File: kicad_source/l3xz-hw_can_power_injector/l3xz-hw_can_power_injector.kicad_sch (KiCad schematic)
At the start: 6 parts

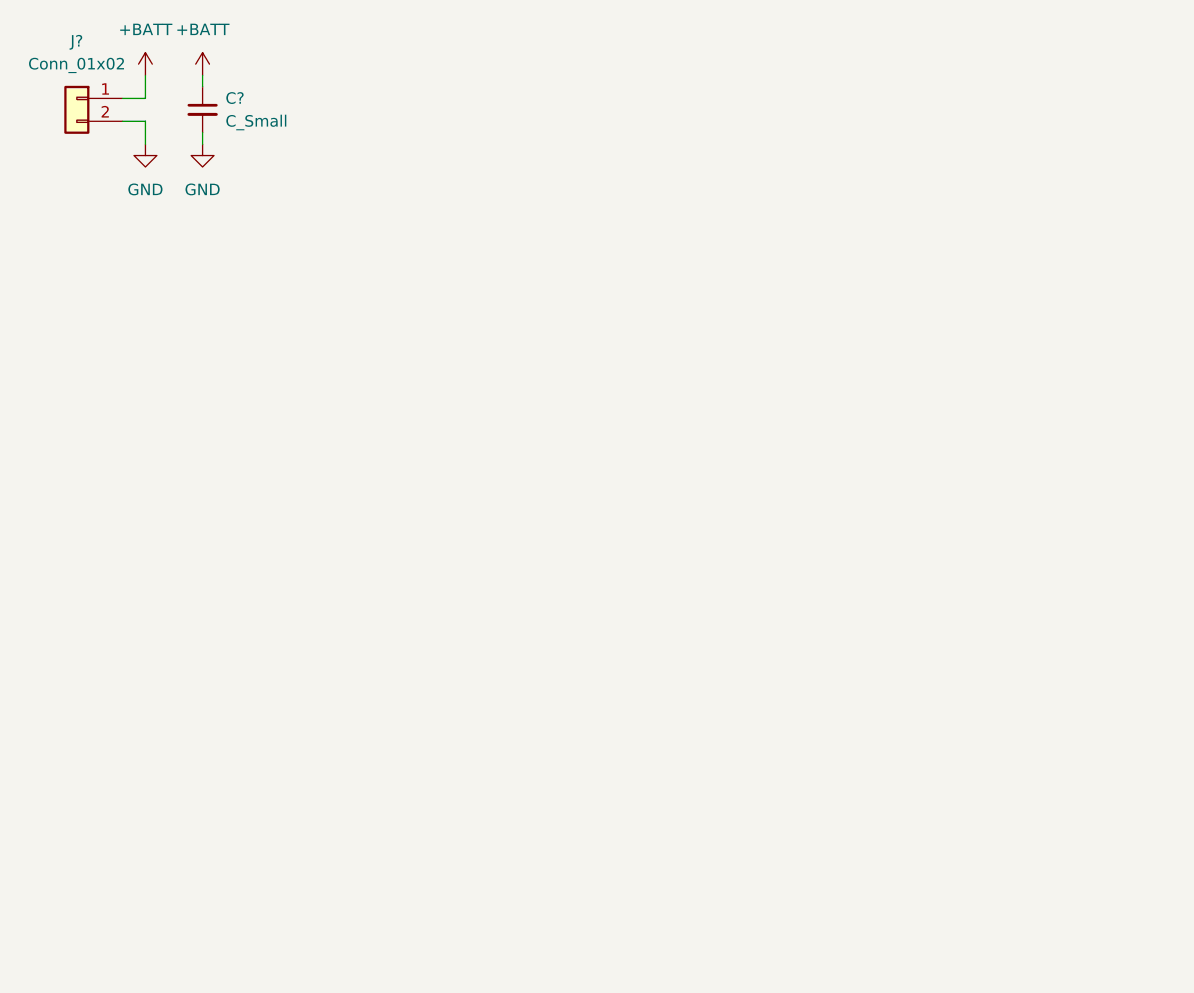
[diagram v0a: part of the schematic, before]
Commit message: added switching regulator to schematic
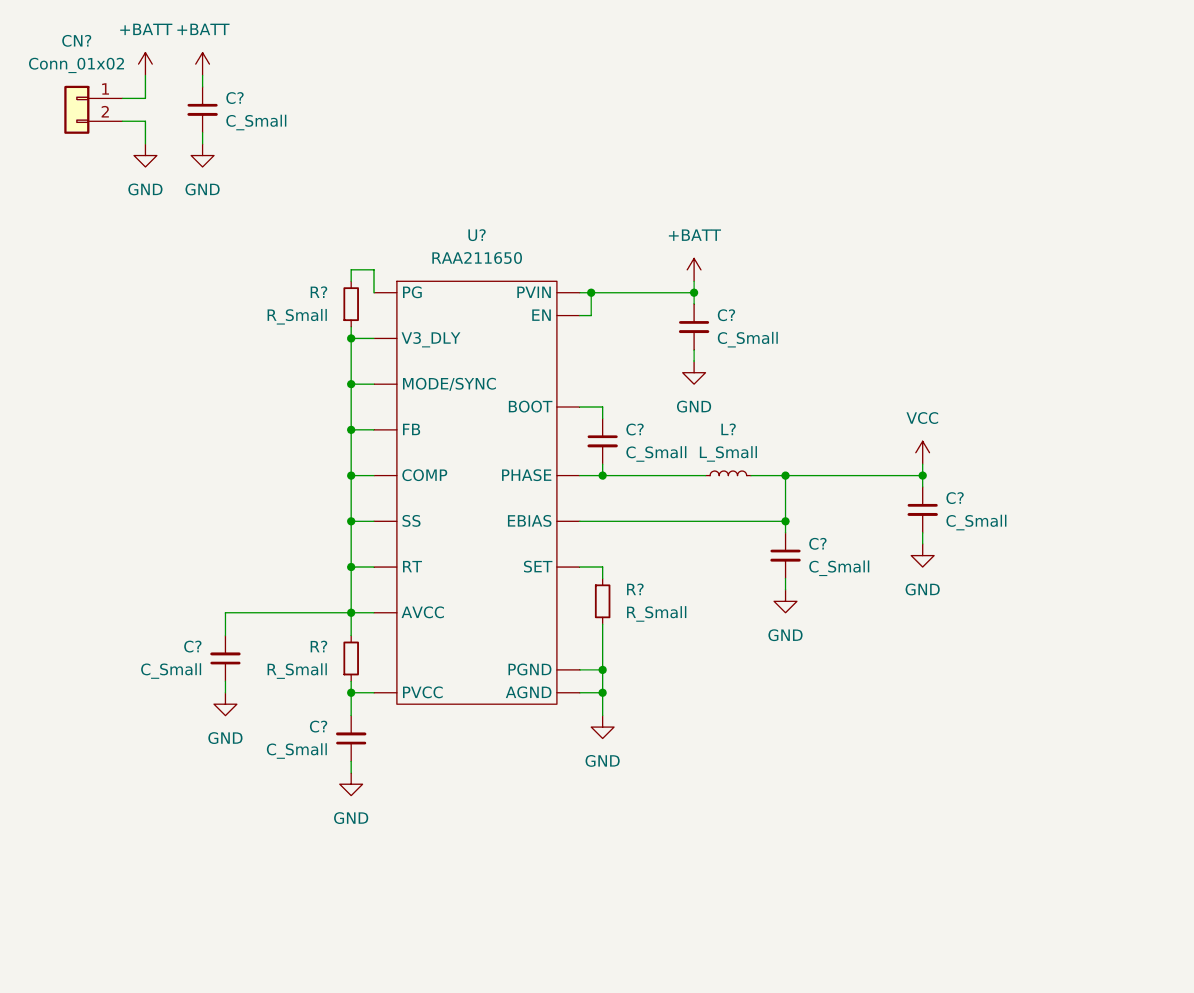
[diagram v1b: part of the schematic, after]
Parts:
- added C? (x6): C_Small, symbol Device:C_Small
- added L?: L_Small, symbol Device:L_Small
- added R? (x3): R_Small, symbol Device:R_Small
- added U?: RAA211650, symbol generationmake:RAA211650
- gave numbers to parts that had none: 1
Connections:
- net +BATT: now also C?.1, U?. (V3_DLY)
- net GND: now also C?.1, C?.1, C?.2, C?.2, C?.2, R?.2, U?. (V3_DLY)
- net VCC: now also C?.1, C?.1, L?.2, U?. (V3_DLY)
- new net: C?.2, R?.1, R?.2, U?. (V3_DLY)
- new net: C?.2, R?.1, U?. (V3_DLY)
- new net: C?.2, L?.1, U?. (V3_DLY)
- new net: C?.1, U?. (V3_DLY)
- new net: R?.2, U?. (V3_DLY)
- new net: R?.1, U?. (V3_DLY)

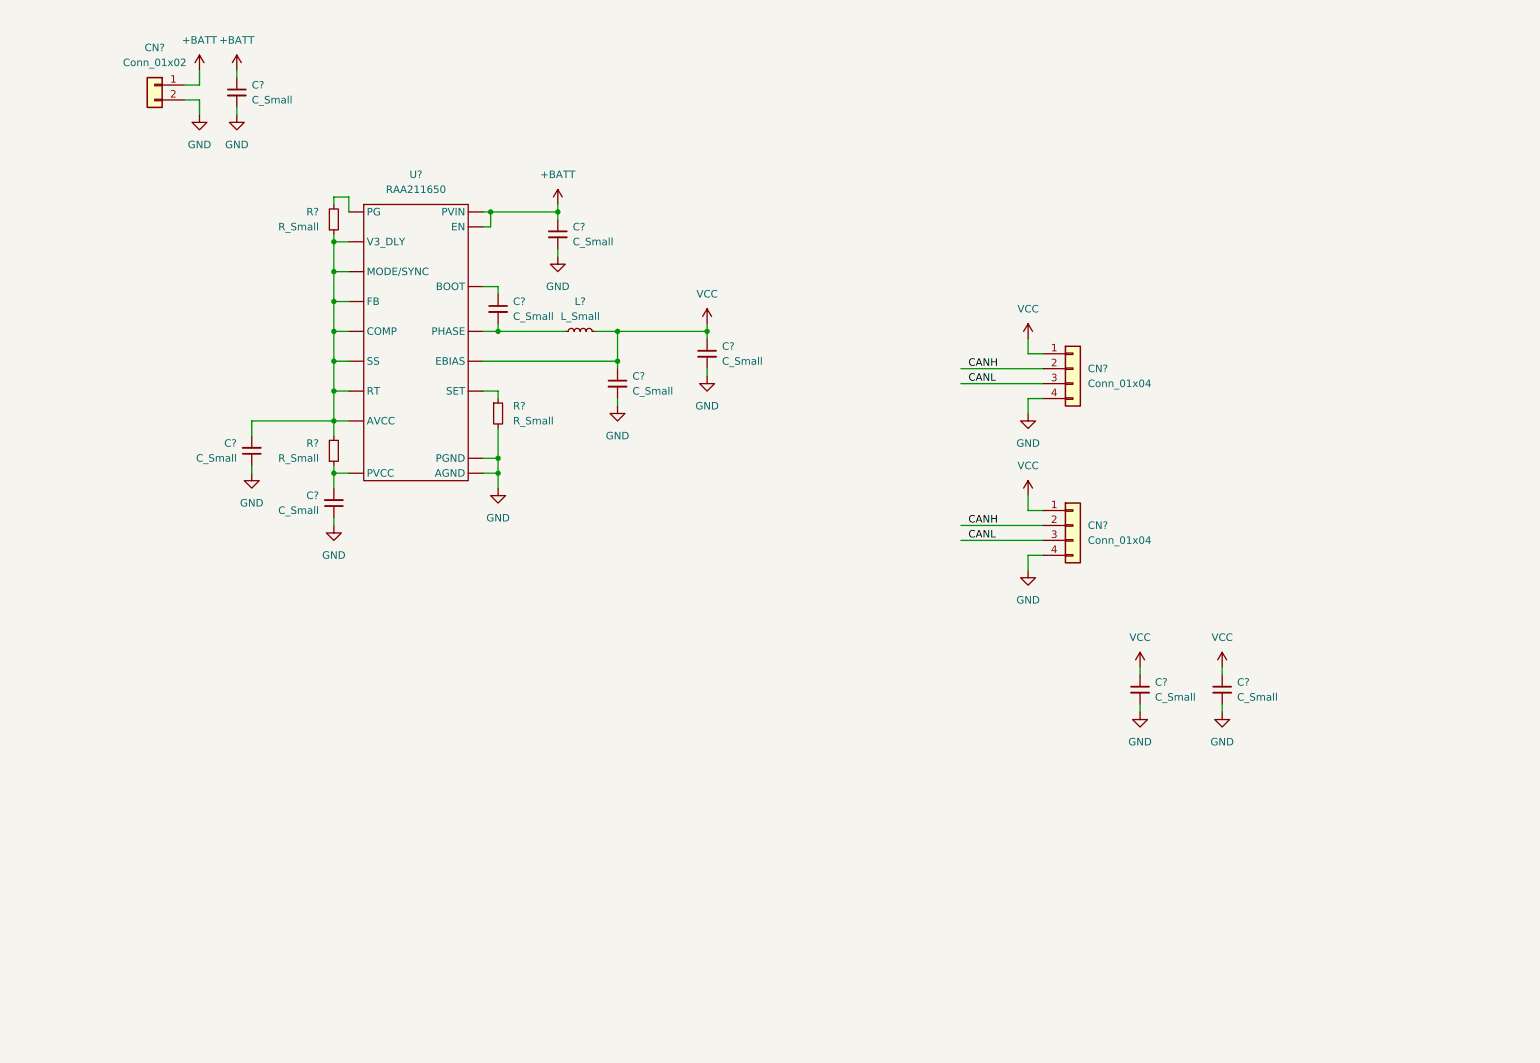
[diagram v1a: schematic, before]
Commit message: updated and annotated schematic
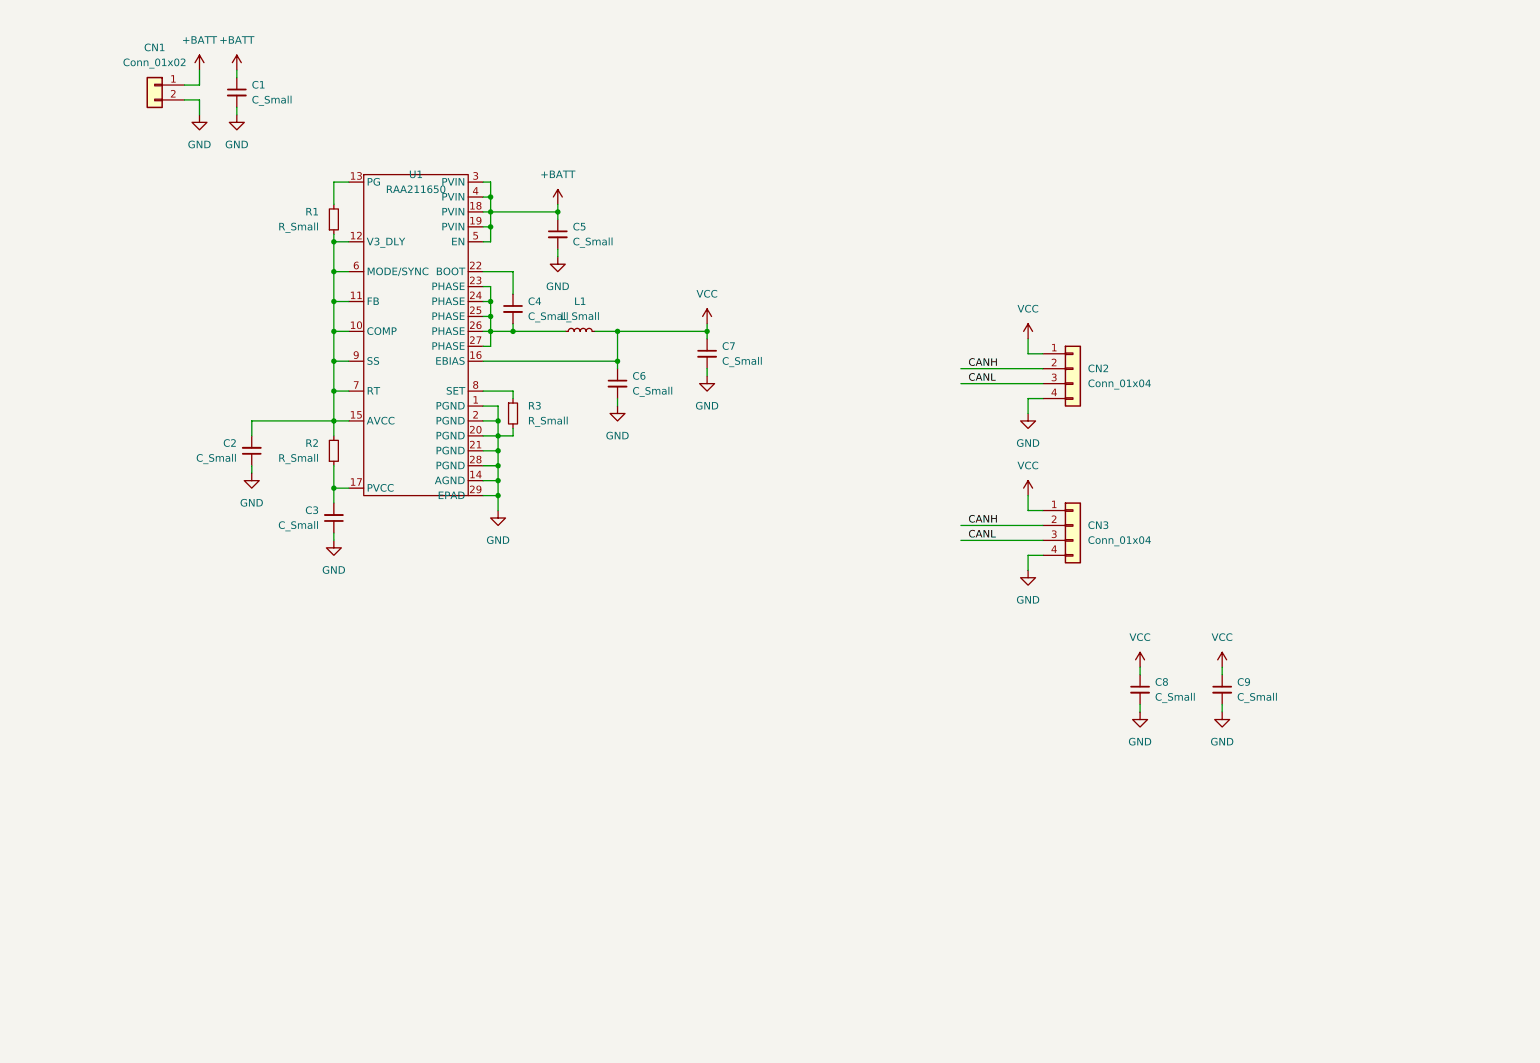
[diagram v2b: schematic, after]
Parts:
- C1, C5, C7, C8: renamed from C?; footprint (none) -> Capacitor_SMD:C_1210_3225Metric
- C2, C3, C4, C6, C9: renamed from C?; footprint (none) -> Capacitor_SMD:C_0603_1608Metric
- CN1: renamed from CN?; footprint (none) -> Connector_Wago:Wago_734-132_1x02_P3.50mm_Vertical
- CN2, CN3: renamed from CN?; footprint (none) -> Connector_JST:JST_GH_BM04B-GHS-TBT_1x04-1MP_P1.25mm_Vertical
- L1: renamed from L?; footprint (none) -> Inductor_SMD:L_7.3x7.3_H4.5
- R1, R2, R3: renamed from R?; footprint (none) -> Resistor_SMD:R_0603_1608Metric
- U1: renamed from U?; footprint (none) -> Package_DFN_QFN:QFN-28-1EP_4x5mm_P0.5mm_EP2.65x3.65mm
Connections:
- net +BATT: now also U1.18 (PVIN), U1.19 (PVIN), U1.3 (PVIN), U1.4 (PVIN), U1.5 (EN); no longer U1. (V3_DLY)
- net GND: now also U1.1 (PGND), U1.14 (AGND), U1.2 (PGND), U1.20 (PGND), U1.21 (PGND), U1.28 (PGND), U1.29 (EPAD); no longer U1. (V3_DLY)
- net VCC: now also U1.16 (EBIAS); no longer U1. (V3_DLY)
- net at C2.2, R1.1, R2.2: now also U1.10 (COMP), U1.11 (FB), U1.12 (V3_DLY), U1.15 (AVCC), U1.6 (MODE/SYNC), U1.7 (RT), U1.9 (SS); no longer U1. (V3_DLY)
- net at C3.2, R2.1: now also U1.17 (PVCC); no longer U1. (V3_DLY)
- net at C4.2, L1.1: now also U1.23 (PHASE), U1.24 (PHASE), U1.25 (PHASE), U1.26 (PHASE), U1.27 (PHASE); no longer U1. (V3_DLY)
- net at C4.1: now also U1.22 (BOOT); no longer U1. (V3_DLY)
- net at R1.2: now also U1.13 (PG); no longer U1. (V3_DLY)
- net at R3.1: now also U1.8 (SET); no longer U1. (V3_DLY)
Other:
- moved on the sheet: C3, C4, R3

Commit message: started layout
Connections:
- net AVCC: now reaches C2.2, R1.1, R2.2, U1.10 (COMP), U1.11 (FB), U1.12 (V3_DLY), U1.15 (AVCC), U1.6 (MODE/SYNC), U1.7 (RT), U1.9 (SS)
- net PVCC: now reaches C3.2, R2.1, U1.17 (PVCC)
- net PHASE: now reaches C4.2, L1.1, U1.23 (PHASE), U1.24 (PHASE), U1.25 (PHASE), U1.26 (PHASE), U1.27 (PHASE)
- net BOOT: now reaches C4.1, U1.22 (BOOT)
- net PG: now reaches R1.2, U1.13 (PG)
- net SET: now reaches R3.1, U1.8 (SET)
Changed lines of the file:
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@@
+    (effects (font (size 1.27 1.27)) (justify left bottom))
+  )
+  (label "PVCC" (at 71.12 96.52 0)
+    (effects (font (size 1.27 1.27)) (justify left bottom))
+  )
+  (label "PHASE" (at 102.87 69.85 0)
+    (effects (font (size 1.27 1.27)) (justify left bottom))
+  )
+  (label "SET" (at 97.79 80.01 0)
     (effects (font (size 1.27 1.27)) (justify left bottom))
   )
@@
     (effects (font (size 1.27 1.27)) (justify left bottom))
   )
+  (label "AVCC" (at 60.96 85.09 0)
+    (effects (font (size 1.27 1.27)) (justify left bottom))
+  )
+  (label "PG" (at 69.85 44.45 0)
+    (effects (font (size 1.27 1.27)) (justify left bottom))
+  )
+  (label "BOOT" (at 97.79 59.69 0)
+    (effects (font (size 1.27 1.27)) (justify left bottom))
+  )

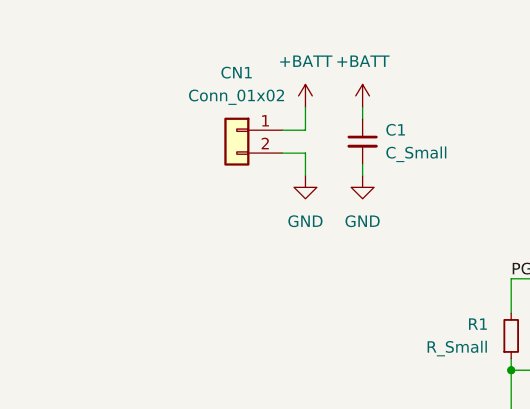
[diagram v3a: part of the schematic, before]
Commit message: added Powerpole connector
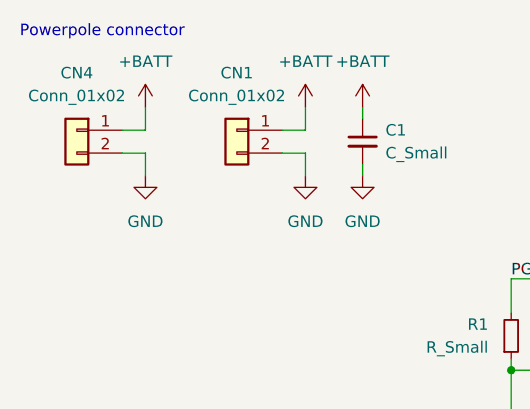
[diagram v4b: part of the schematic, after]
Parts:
- added CN4: Conn_01x02, generationmake:POWERPOLE_2, symbol Connector_Generic:Conn_01x02
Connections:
- net +BATT: now also CN4.1 (Pin_1)
- net GND: now also CN4.2 (Pin_2)
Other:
- note added: "Powerpole connector"
- company: (none) -> 107-systems
- title: (none) -> l3xz-hw_can_power_injector
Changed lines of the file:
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@@
 (kicad_sch (version 20211123) (generator eeschema)
   (paper "A4")
+  (title_block
+    (title "l3xz-hw_can_power_injector")
+    (date "2022-10-25")
+    (rev "0.1")
+    (company "107-systems")
+  )
   (junction (at 96.52 49.53) (diameter 0) (color 0 0 0 0)
   )
@@
     (stroke (width 0) (type default) (color 0 0 0 0))
   )
+  (wire (pts (xy 29.21 27.94) (xy 29.21 25.4))
+    (stroke (width 0) (type default) (color 0 0 0 0))
+  )
   (wire (pts (xy 187.96 73.66) (xy 187.96 71.12))
     (stroke (width 0) (type default) (color 0 0 0 0))
@@
     (stroke (width 0) (type default) (color 0 0 0 0))
   )
+  (wire (pts (xy 26.67 30.48) (xy 29.21 30.48))
+    (stroke (width 0) (type default) (color 0 0 0 0))
+  )
   (wire (pts (xy 96.52 64.77) (xy 96.52 67.31))
     (stroke (width 0) (type default) (color 0 0 0 0))
@@
     (stroke (width 0) (type default) (color 0 0 0 0))
   )
+  (wire (pts (xy 29.21 30.48) (xy 29.21 33.02))
+    (stroke (width 0) (type default) (color 0 0 0 0))
+  )
   (wire (pts (xy 95.25 92.71) (xy 97.79 92.71))
     (stroke (width 0) (type default) (color 0 0 0 0))
@@
     (stroke (width 0) (type default) (color 0 0 0 0))
   )
+  (wire (pts (xy 26.67 27.94) (xy 29.21 27.94))
+    (stroke (width 0) (type default) (color 0 0 0 0))
+  )
   (wire (pts (xy 95.25 49.53) (xy 96.52 49.53))
     (stroke (width 0) (type default) (color 0 0 0 0))
@@
   (wire (pts (xy 95.25 85.09) (xy 97.79 85.09))
     (stroke (width 0) (type default) (color 0 0 0 0))
+  )
+  (text "Powerpole connector" (at 15.24 17.78 0)
+    (effects (font (size 1.27 1.27)) (justify left bottom))
   )
   (label "CANH" (at 177.8 102.87 0)
@@
     (pin "1")
   )
+  (symbol (lib_id "Connector_Generic:Conn_01x02") (at 21.59 27.94 0) (mirror y) (unit 1)
+    (in_bom yes) (on_board yes) (fields_autoplaced)
+    (property "Reference" "CN4" (id 0) (at 21.59 21.59 0))
+    (property "Value" "Conn_01x02" (id 1) (at 21.59 24.13 0))
+    (property "Footprint" "generationmake:POWERPOLE_2" (id 2) (at 21.59 27.94 0)
+      (effects (font (size 1.27 1.27)) hide)
+    )
+    (property "Datasheet" "~" (id 3) (at 21.59 27.94 0)
+      (effects (font (size 1.27 1.27)) hide)
+    )
+    (pin "1")
+    (pin "2")
+  )
   (symbol (lib_id "power:GND") (at 55.88 93.98 0) (unit 1)
     (in_bom yes) (on_board yes) (fields_autoplaced)
@@
     )
     (property "Datasheet" "" (id 3) (at 53.34 33.02 0)
+      (effects (font (size 1.27 1.27)) hide)
+    )
+    (pin "1")
+  )
+  (symbol (lib_id "power:+BATT") (at 29.21 25.4 0) (unit 1)
+    (in_bom yes) (on_board yes) (fields_autoplaced)
+    (property "Reference" "#PWR021" (id 0) (at 29.21 29.21 0)
+      (effects (font (size 1.27 1.27)) hide)
+    )
+    (property "Value" "+BATT" (id 1) (at 29.21 20.32 0))
+    (property "Footprint" "" (id 2) (at 29.21 25.4 0)
+      (effects (font (size 1.27 1.27)) hide)
+    )
+    (property "Datasheet" "" (id 3) (at 29.21 25.4 0)
+      (effects (font (size 1.27 1.27)) hide)
+    )
+    (pin "1")
+  )
+  (symbol (lib_id "power:GND") (at 29.21 33.02 0) (unit 1)
+    (in_bom yes) (on_board yes) (fields_autoplaced)
+    (property "Reference" "#PWR022" (id 0) (at 29.21 39.37 0)
+      (effects (font (size 1.27 1.27)) hide)
+    )
+    (property "Value" "GND" (id 1) (at 29.21 38.1 0))
+    (property "Footprint" "" (id 2) (at 29.21 33.02 0)
+      (effects (font (size 1.27 1.27)) hide)
+    )
+    (property "Datasheet" "" (id 3) (at 29.21 33.02 0)
       (effects (font (size 1.27 1.27)) hide)
     )
@@
       (reference "#PWR020") (unit 1) (value "GND") (footprint "")
     )
+    (path "/e83e49ee-dd3d-4e0d-8a22-d49f6f978b87"
+      (reference "#PWR021") (unit 1) (value "+BATT") (footprint "")
+    )
+    (path "/ee8c5056-6ab9-462a-98e4-a73bec92a972"
+      (reference "#PWR022") (unit 1) (value "GND") (footprint "")
+    )
     (path "/5fed680c-7375-4ebc-bb86-a241d3c8e39a"
       (reference "C1") (unit 1) (value "C_Small") (footprint "Capacitor_SMD:C_1210_3225Metric")
@@
       (reference "CN3") (unit 1) (value "Conn_01x04") (footprint "Connector_JST:JST_GH_BM04B-GHS-TBT_1x04-1MP_P1.25mm_Vertical")
     )
+    (path "/8a3827e6-26b6-4873-9005-56e501165c36"
+      (reference "CN4") (unit 1) (value "Conn_01x02") (footprint "generationmake:POWERPOLE_2")
+    )
     (path "/2f54f438-5d34-4db6-a425-bb6ed0e0f809"
